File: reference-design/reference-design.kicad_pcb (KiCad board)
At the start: 2 copper layers, 104 x 83.9 mm, 30 parts

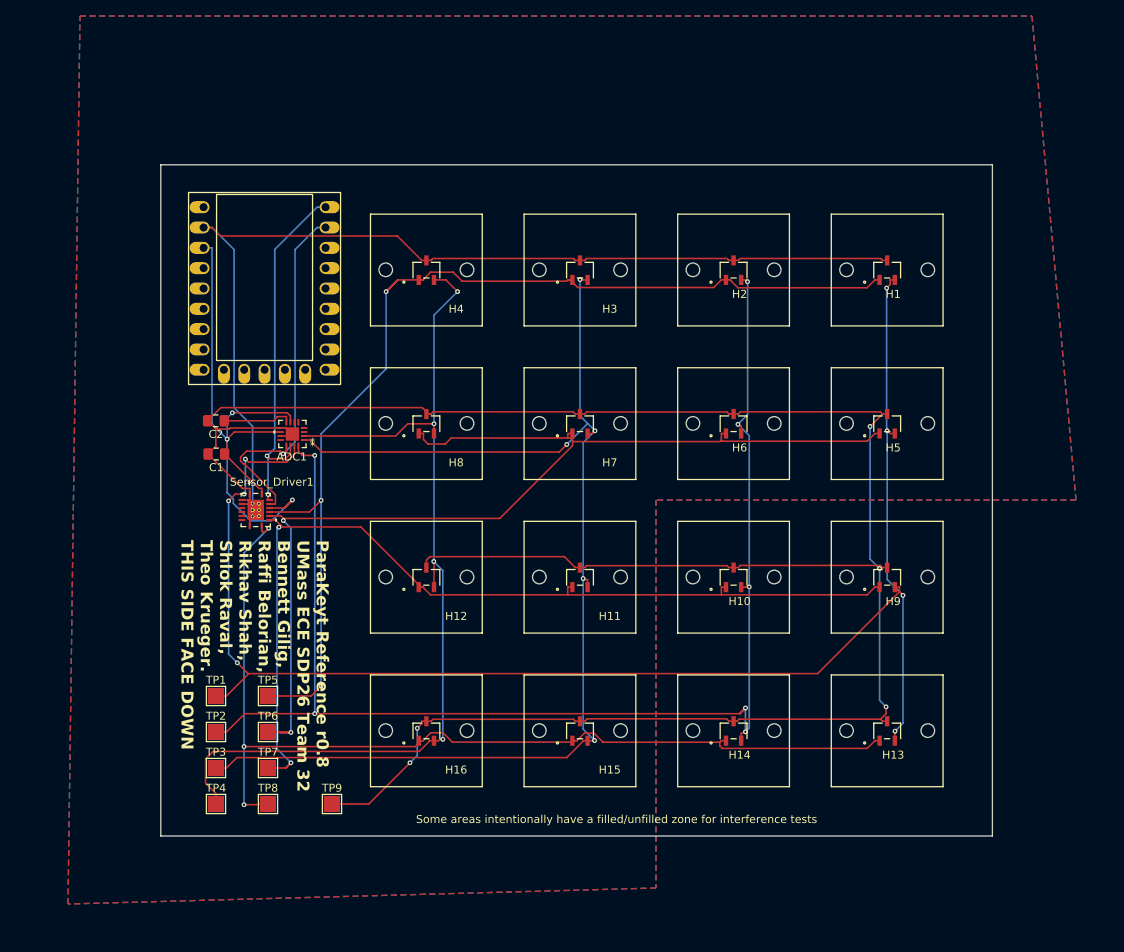
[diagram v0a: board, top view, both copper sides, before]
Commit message: replace led driver with another ADC (to be used as gpio to drive MOSFETs)
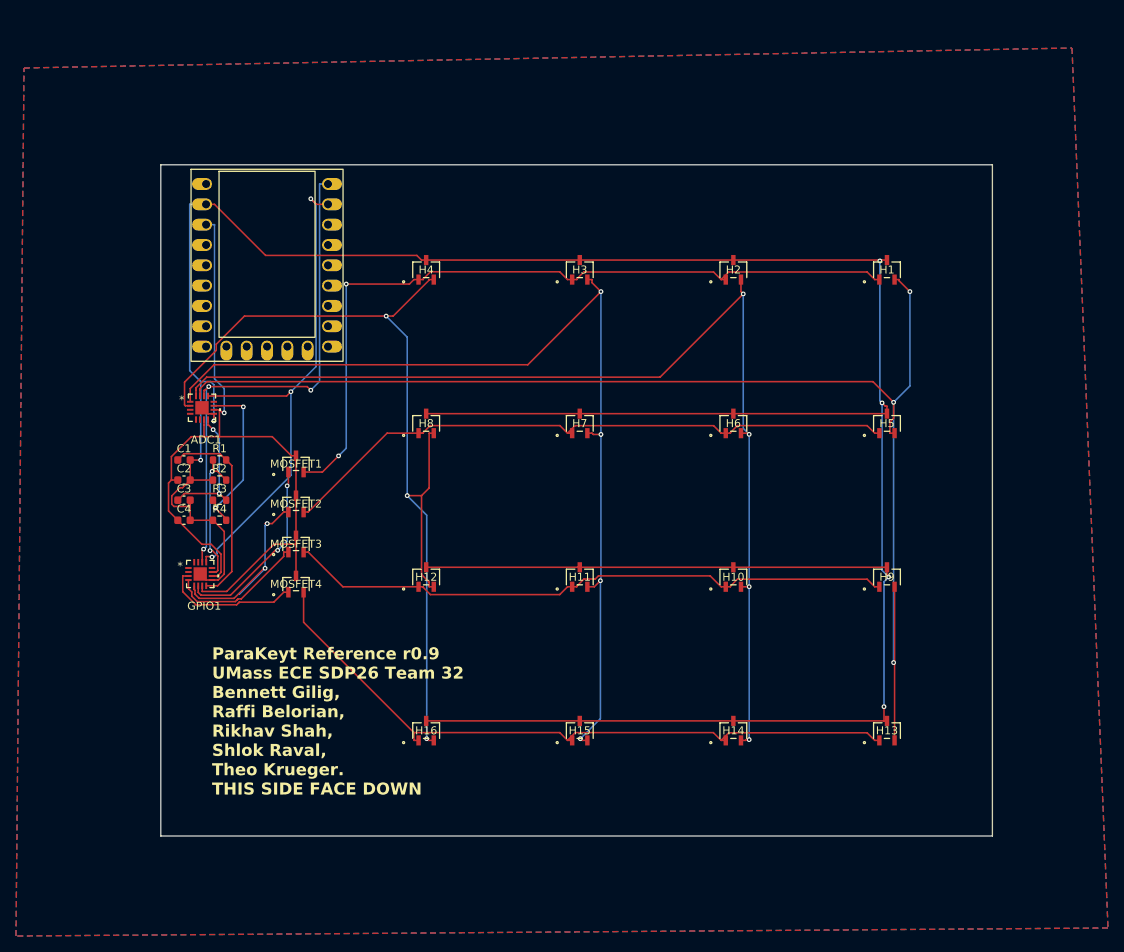
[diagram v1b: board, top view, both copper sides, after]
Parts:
- removed Sensor_Driver1: TLC59108IRGYR, TLC59208FIRGYR:RGY16_2P55X2P05
- removed TP1: col0, TestPoint:TestPoint_Pad_2.0x2.0mm
- removed TP2: col1, TestPoint:TestPoint_Pad_2.0x2.0mm
- removed TP3: col2, TestPoint:TestPoint_Pad_2.0x2.0mm
- removed TP4: col3, TestPoint:TestPoint_Pad_2.0x2.0mm
- removed TP5: row0, TestPoint:TestPoint_Pad_2.0x2.0mm
- removed TP6: row1, TestPoint:TestPoint_Pad_2.0x2.0mm
- removed TP7: row2, TestPoint:TestPoint_Pad_2.0x2.0mm
- removed TP8: row3, TestPoint:TestPoint_Pad_2.0x2.0mm
- removed TP9: GND, TestPoint:TestPoint_Pad_2.0x2.0mm
- added C3: 2uF, Capacitor_SMD:C_0603_1608Metric, F.Cu at (15.0, 54.0)
- added C4: 2uF, Capacitor_SMD:C_0603_1608Metric, F.Cu at (15.0, 56.5)
- added GPIO1: TLA2528IRTER, TLA2528IRTER:WQFN16_RTE_TEX, F.Cu at (17.0, 63.2)
- added MOSFET1: SI2342DS-T1-GE3, SI2342DS-T1-GE3:SOT-23_TO-236_VIS, F.Cu at (29.0, 49.5)
- added MOSFET2: SI2342DS-T1-GE3, SI2342DS-T1-GE3:SOT-23_TO-236_VIS, F.Cu at (29.0, 54.5)
- added MOSFET3: SI2342DS-T1-GE3, SI2342DS-T1-GE3:SOT-23_TO-236_VIS, F.Cu at (29.0, 59.5)
- added MOSFET4: SI2342DS-T1-GE3, SI2342DS-T1-GE3:SOT-23_TO-236_VIS, F.Cu at (29.0, 64.5)
- added R1: 11K, Resistor_SMD:R_0603_1608Metric, F.Cu at (19.4, 49.0)
- added R2: DNP, Resistor_SMD:R_0603_1608Metric, F.Cu at (19.4, 51.5)
- added R3: 0, Resistor_SMD:R_0603_1608Metric, F.Cu at (19.4, 54.0)
- added R4: DNP, Resistor_SMD:R_0603_1608Metric, F.Cu at (19.4, 56.5)
- C1, C2: footprint Capacitor_SMD:C_0805_2012Metric_Pad1.18x1.45mm_HandSolder -> Capacitor_SMD:C_0603_1608Metric
- H1, H10, H13, H14, H2, H5, H6, H9: footprint AH49FNTR_G1:SC59_DIO_KeyswitchOutline_NoRuleArea -> AH49FNTR_G1:SC59_DIO
- H11, H12, H15, H16, H3, H4, H7, H8: footprint AH49FNTR_G1:SC59_DIO_KeyswitchOutline -> AH49FNTR_G1:SC59_DIO
- moved ADC1 11.8 mm to (17.2, 42.5), turned to 0 degrees
- moved C2 8.41 mm to (15.0, 51.5), turned to 0 degrees
- moved C1 4.11 mm to (15.0, 49.0), turned to 0 degrees
- moved MCU1 2.92 mm to (25.4, 24.7)
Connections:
- net row0 renamed Net-(H1-VCC)
- net row1 renamed Net-(H5-VCC)
- net row2 renamed Net-(H10-VCC)
- net row3 renamed Net-(H13-VCC)
- ADC1 pad 11: GND -> Net-(ADC1-ADDR)
- C1 pad 1: +3.3V -> Net-(GPIO1-DECAP)
- C2 pad 1: Net-(ADC1-DECAP) -> +3.3V
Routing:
- net Net-(H5-VCC): track 140.2 -> 79.1 mm, vias 2 -> 0
- net Net-(H10-VCC): track 122.4 -> 76.6 mm, vias 2 -> 0
- net Net-(H1-VCC): track 140.3 -> 97.0 mm, vias 3 -> 2
- net Net-(H13-VCC): track 124.7 -> 86.1 mm, vias 3 -> 0
- net col1: track 172.1 -> 135.4 mm, vias 7 -> 4
- net row1: track 0.00 -> 30.7 mm, vias 0 -> 2
- net col0: track 190.5 -> 162.9 mm, vias 8 -> 3
- net col2: track 149.5 -> 122.2 mm, vias 5 -> 4
- net GND: track 422.0 -> 395.8 mm, vias 5 -> 6
- net Net-(GPIO1-DECAP): track 0.00 -> 24.9 mm
- net row0: track 0.00 -> 23.6 mm, vias 0 -> 2
- net Net-(ADC1-ADDR): track 0.00 -> 21.0 mm, vias 0 -> 2
- net +3.3V: track 80.3 -> 99.7 mm, vias 3 -> 1
- net i2c0_sda: track 44.8 -> 64.1 mm, vias 2 -> 3
- net i2c0_scl: track 46.6 -> 65.0 mm, vias 1 -> 3
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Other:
- board text added: "ParaKeyt Reference r0.9 UMass ECE SDP26 Team 32 Bennett Gilig, Raffi Belorian, Rikhav Shah, Shlok Raval, Theo Krueger. THIS SIDE FACE DOWN"
- board text removed: "ParaKeyt Reference r0.8 UMass ECE SDP26 Team 32 Bennett Gilig, Raffi Belorian, Rikhav Shah, Shlok Raval, Theo Krueger. THIS SIDE FACE DOWN"
- board text removed: "Some areas intentionally have a filled/unfilled zone for interference tests"
